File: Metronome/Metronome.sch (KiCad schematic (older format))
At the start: 48 parts, among them P1 CONN_01X02, P3 CONN_01X05, SW1 SW_PUSH, SW2 SW_PUSH, SW3 SW_PUSH, SW4 SW_PUSH, SW5 SW_PUSH, SW7 SWITCH_INV, T1 BSS138, T2 BSS83P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

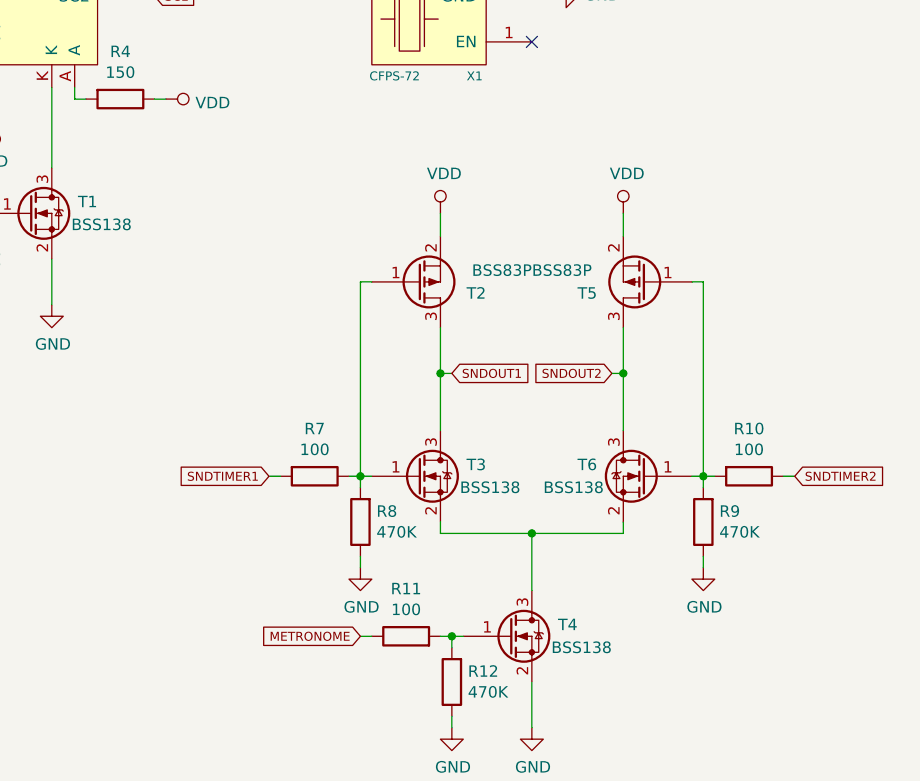
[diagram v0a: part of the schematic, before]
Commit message: PCB Simplification
SOme elements on PCB are unnecessary.
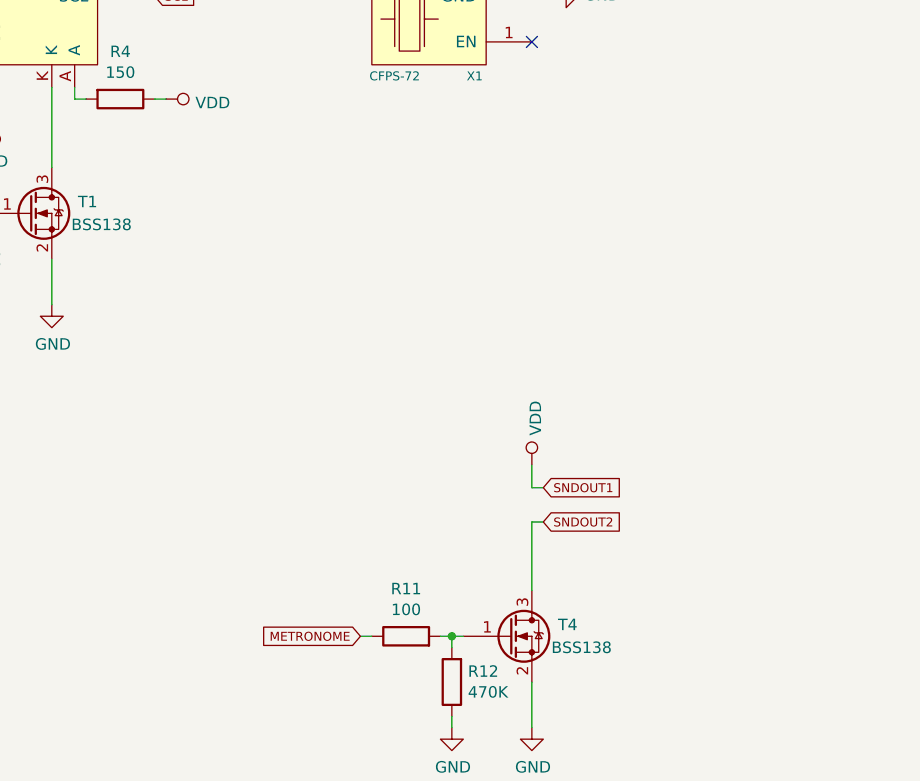
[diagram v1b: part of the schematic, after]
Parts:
- removed R10, R7: 100, Resistors_SMD:R_0603_HandSoldering, symbol R
- removed R8, R9: 470K, Resistors_SMD:R_0603_HandSoldering, symbol R
- removed T2, T5: BSS83P, TO_SOT_Packages_SMD:SOT-23_Handsoldering, symbol Q_PMOS_GSD
- removed T3, T6: BSS138, TO_SOT_Packages_SMD:SOT-23_Handsoldering, symbol Q_NMOS_GSD
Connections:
- net SNDOUT1 is gone; now on net VCC: R19.2
- net SNDOUT2: now also T4.3 (D)
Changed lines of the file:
@@
 Text GLabel 5200 2750 2    39   Input ~ 0
-METRONOME
-Text GLabel 8550 4000 0    39   Input ~ 0
 METRONOME
 $Comp
@@
 	-1   0    0    1
 $EndComp
-Text GLabel 8150 3300 0    39   Input ~ 0
-SNDTIMER1
 Text GLabel 5200 1650 2    39   Input ~ 0
 SNDTIMER1
-$Comp
-L VDD #PWR029
-U 1 1 57958A3B
-P 8900 2150
-F 0 "#PWR029" H 8900 2000 50  0001 C CNN
-F 1 "VDD" H 8917 2323 50  0000 C CNN
-F 2 "" H 8900 2150 50  0000 C CNN
-F 3 "" H 8900 2150 50  0000 C CNN
-	1    8900 2150
-	1    0    0    -1
-$EndComp
-$Comp
-L VDD #PWR030
-U 1 1 57958C88
-P 9700 2150
-F 0 "#PWR030" H 9700 2000 50  0001 C CNN
-F 1 "VDD" H 9717 2323 50  0000 C CNN
-F 2 "" H 9700 2150 50  0000 C CNN
-F 3 "" H 9700 2150 50  0000 C CNN
-	1    9700 2150
-	1    0    0    -1
-$EndComp
 $Comp
 L R R11
@@
 	1    0    0    -1
 $EndComp
-$Comp
-L R R7
-U 1 1 5795A29A
-P 8350 3300
-F 0 "R7" V 8143 3300 50  0000 C CNN
-F 1 "100" V 8234 3300 50  0000 C CNN
-F 2 "Resistors_SMD:R_0603_HandSoldering" V 8280 3300 50  0001 C CNN
-F 3 "" H 8350 3300 50  0000 C CNN
-	1    8350 3300
-	0    1    1    0
-$EndComp
-$Comp
-L R R8
-U 1 1 5795A4D7
-P 8550 3500
-F 0 "R8" H 8480 3454 50  0000 R CNN
-F 1 "470K" H 8480 3545 50  0000 R CNN
-F 2 "Resistors_SMD:R_0603_HandSoldering" V 8480 3500 50  0001 C CNN
-F 3 "" H 8550 3500 50  0000 C CNN
-	1    8550 3500
-	-1   0    0    1
-$EndComp
-$Comp
-L GND #PWR032
-U 1 1 5795A849
-P 8550 3700
-F 0 "#PWR032" H 8550 3450 50  0001 C CNN
-F 1 "GND" H 8555 3527 50  0000 C CNN
-F 2 "" H 8550 3700 50  0000 C CNN
-F 3 "" H 8550 3700 50  0000 C CNN
-	1    8550 3700
-	1    0    0    -1
-$EndComp
-$Comp
-L R R9
-U 1 1 5795B0C7
-P 10050 3500
-F 0 "R9" H 9980 3454 50  0000 R CNN
-F 1 "470K" H 9980 3545 50  0000 R CNN
-F 2 "Resistors_SMD:R_0603_HandSoldering" V 9980 3500 50  0001 C CNN
-F 3 "" H 10050 3500 50  0000 C CNN
-	1    10050 3500
-	-1   0    0    1
-$EndComp
-$Comp
-L GND #PWR033
-U 1 1 5795B1AB
-P 10050 3700
-F 0 "#PWR033" H 10050 3450 50  0001 C CNN
-F 1 "GND" H 10055 3527 50  0000 C CNN
-F 2 "" H 10050 3700 50  0000 C CNN
-F 3 "" H 10050 3700 50  0000 C CNN
-	1    10050 3700
-	1    0    0    -1
-$EndComp
-$Comp
-L R R10
-U 1 1 5795B70D
-P 10250 3300
-F 0 "R10" V 10043 3300 50  0000 C CNN
-F 1 "100" V 10134 3300 50  0000 C CNN
-F 2 "Resistors_SMD:R_0603_HandSoldering" V 10180 3300 50  0001 C CNN
-F 3 "" H 10250 3300 50  0000 C CNN
-	1    10250 3300
-	0    1    1    0
-$EndComp
-Text GLabel 10450 3300 2    39   Input ~ 0
-SNDTIMER2
-Text GLabel 8950 2850 2    39   Input ~ 0
-SNDOUT1
-Text GLabel 9650 2850 0    39   Input ~ 0
+Text GLabel 9350 3500 2    39   Input ~ 0
 SNDOUT2
 $Comp
@@
 $EndComp
 $Comp
-L Q_NMOS_GSD T3
-U 1 1 579D401D
-P 8800 3300
-F 0 "T3" H 9100 3350 50  0000 R CNN
-F 1 "BSS138" H 9250 3250 50  0000 R CNN
-F 2 "TO_SOT_Packages_SMD:SOT-23_Handsoldering" H 9000 3400 50  0001 C CNN
-F 3 "" H 8800 3300 50  0000 C CNN
-	1    8800 3300
-	1    0    0    -1
-$EndComp
-$Comp
-L Q_NMOS_GSD T6
-U 1 1 579D5110
-P 9800 3300
-F 0 "T6" H 10100 3350 50  0000 R CNN
-F 1 "BSS138" H 10250 3250 50  0000 R CNN
-F 2 "TO_SOT_Packages_SMD:SOT-23_Handsoldering" H 10000 3400 50  0001 C CNN
-F 3 "" H 9800 3300 50  0000 C CNN
-	1    9800 3300
-	-1   0    0    -1
-$EndComp
-$Comp
 L Q_NMOS_GSD T4
 U 1 1 579D66A3
@@
 	1    7100 2150
 	1    0    0    -1
-$EndComp
-$Comp
-L Q_PMOS_GSD T2
-U 1 1 579D8846
-P 8800 2450
-F 0 "T2" H 9100 2500 50  0000 R CNN
-F 1 "BSS83P" H 9300 2400 50  0000 R CNN
-F 2 "TO_SOT_Packages_SMD:SOT-23_Handsoldering" H 9000 2550 50  0001 C CNN
-F 3 "" H 8800 2450 50  0000 C CNN
-	1    8800 2450
-	1    0    0    1
-$EndComp
-$Comp
-L Q_PMOS_GSD T5
-U 1 1 579D9330
-P 9800 2450
-F 0 "T5" H 10100 2500 50  0000 R CNN
-F 1 "BSS83P" H 10300 2400 50  0000 R CNN
-F 2 "TO_SOT_Packages_SMD:SOT-23_Handsoldering" H 10000 2550 50  0001 C CNN
-F 3 "" H 9800 2450 50  0000 C CNN
-	1    9800 2450
-	-1   0    0    1
 $EndComp
 $Comp
@@
 	3750 2450 3700 2450
 Wire Wire Line
-	8900 2650 8900 3100
-Wire Wire Line
-	8900 2250 8900 2150
-Wire Wire Line
-	8550 2450 8600 2450
-Wire Wire Line
-	8550 3350 8550 2450
-Wire Wire Line
-	10050 2450 10050 3350
-Wire Wire Line
-	10000 2450 10050 2450
-Wire Wire Line
-	9700 2150 9700 2250
-Wire Wire Line
 	3750 2050 3700 2050
 Wire Wire Line
@@
 	5200 2150 5150 2150
 Wire Wire Line
-	8500 3300 8600 3300
-Wire Wire Line
 	8900 4000 9000 4000
 Wire Wire Line
 	8550 4000 8600 4000
-Wire Wire Line
-	10000 3300 10100 3300
-Wire Wire Line
-	8550 3700 8550 3650
-Connection ~ 8550 3300
-Wire Wire Line
-	10050 3700 10050 3650
-Connection ~ 10050 3300
-Wire Wire Line
-	8150 3300 8200 3300
-Wire Wire Line
-	10450 3300 10400 3300
-Wire Wire Line
-	9700 2650 9700 3100
-Connection ~ 8900 2850
-Connection ~ 9700 2850
-Wire Wire Line
-	8950 2850 8900 2850
-Wire Wire Line
-	9650 2850 9700 2850
 Wire Wire Line
 	8600 5200 9900 5200
@@
 Connection ~ 4750 3700
 Wire Wire Line
-	9300 3550 9300 3800
-Wire Wire Line
-	8900 3550 9700 3550
-Wire Wire Line
-	8900 3550 8900 3500
-Wire Wire Line
-	9700 3550 9700 3500
-Connection ~ 9300 3550
+	9300 3500 9300 3800
 Wire Wire Line
 	9300 4200 9300 4400
@@
 	5150 2750 5200 2750
 NoConn ~ 3700 2450
+Text GLabel 9350 3350 2    39   Input ~ 0
+SNDOUT1
+Text GLabel 8550 4000 0    39   Input ~ 0
+METRONOME
+Wire Wire Line
+	9350 3500 9300 3500
+Wire Wire Line
+	9300 3350 9350 3350
+Wire Wire Line
+	9300 3250 9300 3350
+$Comp
+L VDD #PWR?
+U 1 1 58AE1602
+P 9300 3250
+F 0 "#PWR?" H 9300 3100 50  0001 C CNN
+F 1 "VDD" V 9317 3378 50  0000 L CNN
+F 2 "" H 9300 3250 50  0000 C CNN
+F 3 "" H 9300 3250 50  0000 C CNN
+	1    9300 3250
+	1    0    0    -1
+$EndComp
 $EndSCHEMATC

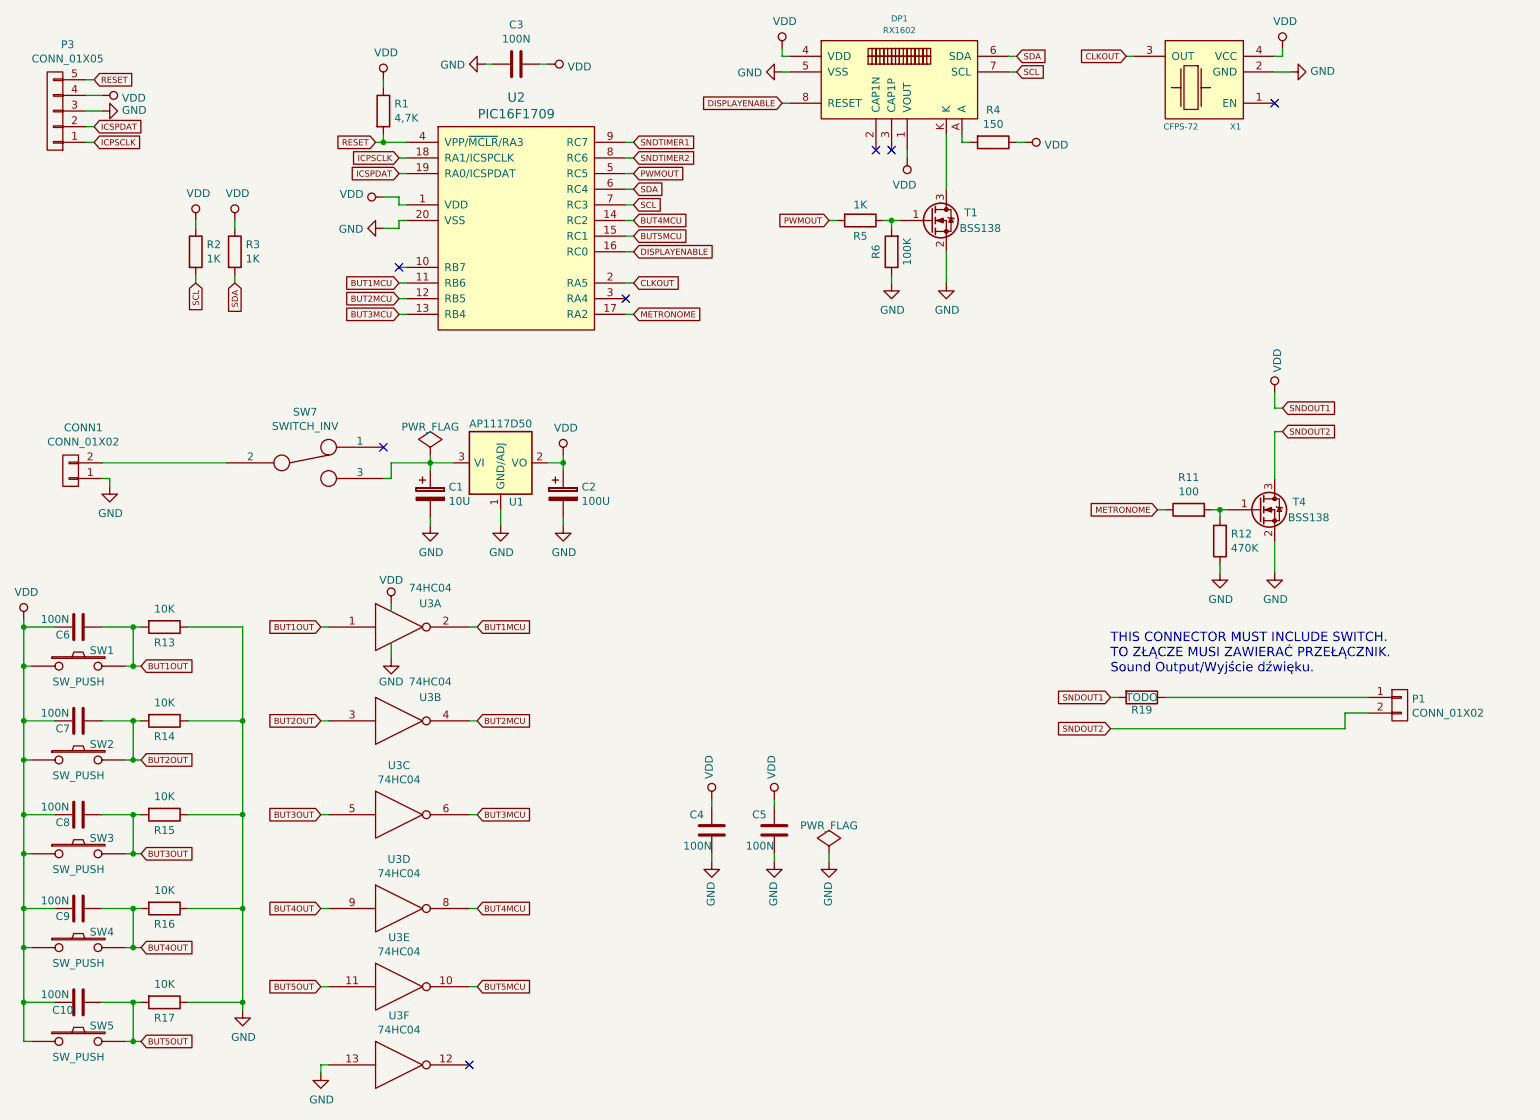
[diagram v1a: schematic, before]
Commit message: Deleting unnecessary traces on PCB
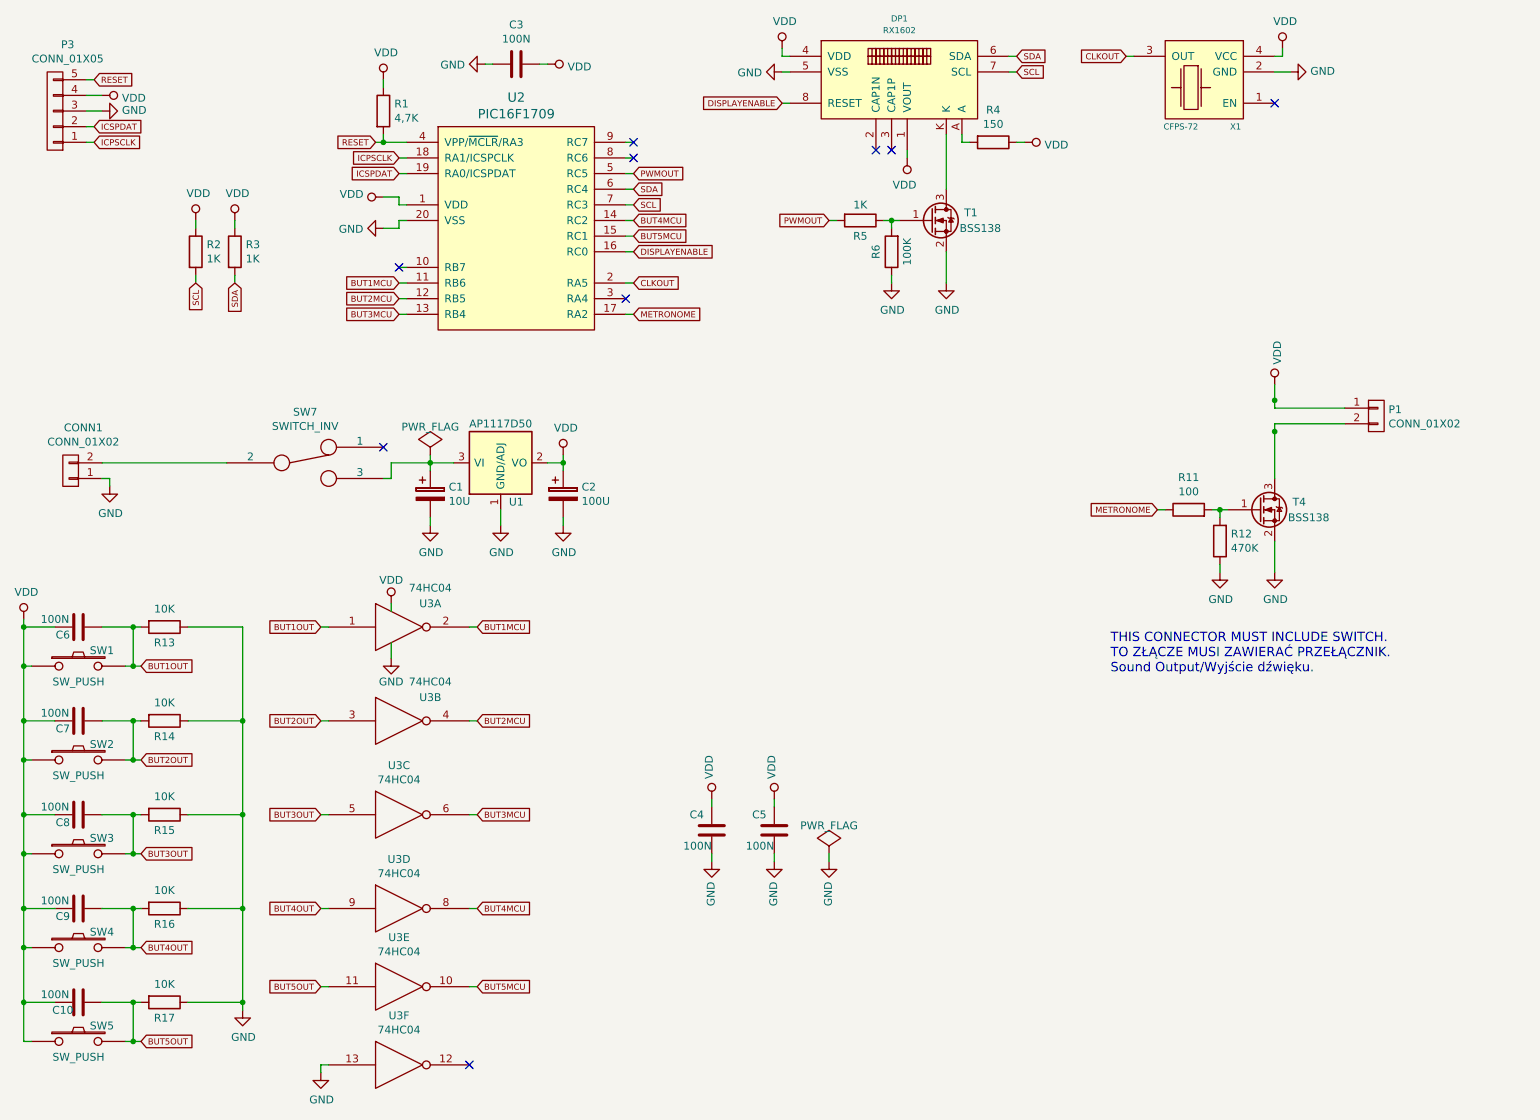
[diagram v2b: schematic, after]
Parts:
- removed R19: TODO, Resistors_SMD:R_0805_HandSoldering, symbol R
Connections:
- net VCC: now also P1.1 (P1)
- net SNDOUT2: no longer names the net of P1.2 (P2), T4.3 (D)
- net SNDTIMER1: no longer names the net of U2.9 (RC7)
- net SNDTIMER2: no longer names the net of U2.8 (RC6)
- no-connect marks 7 -> 9
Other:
- moved on the sheet: P1
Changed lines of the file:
@@
 Text GLabel 6150 1400 0    39   Input ~ 0
 DISPLAYENABLE
-Text GLabel 5200 1750 2    39   Input ~ 0
-SNDTIMER2
 $Comp
 L R R5
@@
 	-1   0    0    1
 $EndComp
-Text GLabel 5200 1650 2    39   Input ~ 0
-SNDTIMER1
 $Comp
 L R R11
@@
 $EndComp
 $Comp
-L GND #PWR031
+L GND #PWR029
 U 1 1 57959876
 P 9300 4400
-F 0 "#PWR031" H 9300 4150 50  0001 C CNN
+F 0 "#PWR029" H 9300 4150 50  0001 C CNN
 F 1 "GND" H 9305 4227 50  0000 C CNN
 F 2 "" H 9300 4400 50  0000 C CNN
@@
 	1    0    0    -1
 $EndComp
-Text GLabel 9350 3500 2    39   Input ~ 0
-SNDOUT2
 $Comp
 L R R12
@@
 $EndComp
 $Comp
-L GND #PWR034
+L GND #PWR030
 U 1 1 5796A8EC
 P 8950 4400
-F 0 "#PWR034" H 8950 4150 50  0001 C CNN
+F 0 "#PWR030" H 8950 4150 50  0001 C CNN
 F 1 "GND" H 8955 4227 50  0000 C CNN
 F 2 "" H 8950 4400 50  0000 C CNN
@@
 $EndComp
 $Comp
-L PWR_FLAG #FLG035
+L PWR_FLAG #FLG031
 U 1 1 5797F436
 P 3900 3650
-F 0 "#FLG035" H 3900 3745 50  0001 C CNN
+F 0 "#FLG031" H 3900 3745 50  0001 C CNN
 F 1 "PWR_FLAG" H 3900 3830 50  0000 C CNN
 F 2 "" H 3900 3650 50  0000 C CNN
@@
 NoConn ~ 3600 3600
 $Comp
-L GND #PWR036
+L GND #PWR032
 U 1 1 57981ADB
 P 6450 6250
-F 0 "#PWR036" H 6450 6000 50  0001 C CNN
+F 0 "#PWR032" H 6450 6000 50  0001 C CNN
 F 1 "GND" V 6455 6122 50  0000 R CNN
 F 2 "" H 6450 6250 50  0000 C CNN
@@
 $EndComp
 $Comp
-L PWR_FLAG #FLG037
+L PWR_FLAG #FLG033
 U 1 1 57981B5C
 P 6450 6200
-F 0 "#FLG037" H 6450 6295 50  0001 C CNN
+F 0 "#FLG033" H 6450 6295 50  0001 C CNN
 F 1 "PWR_FLAG" H 6450 6380 50  0000 C CNN
 F 2 "" H 6450 6200 50  0000 C CNN
@@
 	1    0    0    -1
 $EndComp
-Text GLabel 8250 5200 0    39   Input ~ 0
-SNDOUT1
-Text GLabel 8250 5400 0    39   Input ~ 0
-SNDOUT2
-$Comp
-L VDD #PWR038
+$Comp
+L VDD #PWR034
 U 1 1 57983B16
 P 3650 4600
-F 0 "#PWR038" H 3650 4450 50  0001 C CNN
+F 0 "#PWR034" H 3650 4450 50  0001 C CNN
 F 1 "VDD" H 3650 4750 50  0000 C CNN
 F 2 "" H 3650 4600 50  0000 C CNN
@@
 $EndComp
 $Comp
-L GND #PWR039
+L GND #PWR035
 U 1 1 5798475D
 P 3650 4950
-F 0 "#PWR039" H 3650 4700 50  0001 C CNN
+F 0 "#PWR035" H 3650 4700 50  0001 C CNN
 F 1 "GND" H 3650 4800 50  0000 C CNN
 F 2 "" H 3650 4950 50  0000 C CNN
@@
 	1    0    0    -1
 $EndComp
-$Comp
-L R R19
-U 1 1 579DECB2
-P 8450 5200
-F 0 "R19" V 8530 5200 50  0000 C CNN
-F 1 "TODO" V 8450 5200 50  0000 C CNN
-F 2 "Resistors_SMD:R_0805_HandSoldering" V 8380 5200 50  0001 C CNN
-F 3 "" H 8450 5200 50  0000 C CNN
-	1    8450 5200
-	0    1    1    0
-$EndComp
 NoConn ~ 5150 2650
 Text Notes 8250 5050 0    60   ~ 0
@@
 L CONN_01X02 P1
 U 1 1 57A646B0
-P 10100 5250
-F 0 "P1" H 10178 5291 50  0000 L CNN
-F 1 "CONN_01X02" H 10178 5200 50  0000 L CNN
-F 2 "Pin_Headers:Pin_Header_Straight_1x02" H 10100 5250 50  0001 C CNN
-F 3 "" H 10100 5250 50  0000 C CNN
-	1    10100 5250
+P 9950 3400
+F 0 "P1" H 10028 3441 50  0000 L CNN
+F 1 "CONN_01X02" H 10028 3350 50  0000 L CNN
+F 2 "Pin_Headers:Pin_Header_Straight_1x02" H 9950 3400 50  0001 C CNN
+F 3 "" H 9950 3400 50  0000 C CNN
+	1    9950 3400
 	1    0    0    -1
 $EndComp
@@
 $EndComp
 $Comp
-L GND #PWR040
+L GND #PWR036
 U 1 1 57BF3294
 P 1850 3850
-F 0 "#PWR040" H 1850 3600 50  0001 C CNN
+F 0 "#PWR036" H 1850 3600 50  0001 C CNN
 F 1 "GND" H 1855 3677 50  0000 C CNN
 F 2 "" H 1850 3850 50  0000 C CNN
@@
 $EndComp
 Wire Wire Line
-	8250 5200 8300 5200
-Wire Wire Line
 	3750 2550 3700 2550
 Wire Wire Line
@@
 	8550 4000 8600 4000
 Wire Wire Line
-	8600 5200 9900 5200
-Wire Wire Line
 	8950 4000 8950 4050
 Connection ~ 8950 4000
@@
 Connection ~ 4750 3700
 Wire Wire Line
-	9300 3500 9300 3800
+	9300 3450 9300 3800
 Wire Wire Line
 	9300 4200 9300 4400
-Wire Wire Line
-	9900 5300 9750 5300
-Wire Wire Line
-	9750 5300 9750 5400
-Wire Wire Line
-	9750 5400 8250 5400
 Wire Wire Line
 	6950 1750 6950 1700
@@
 	5150 2750 5200 2750
 NoConn ~ 3700 2450
-Text GLabel 9350 3350 2    39   Input ~ 0
-SNDOUT1
 Text GLabel 8550 4000 0    39   Input ~ 0
 METRONOME
 Wire Wire Line
-	9350 3500 9300 3500
-Wire Wire Line
-	9300 3350 9350 3350
-Wire Wire Line
-	9300 3250 9300 3350
-$Comp
-L VDD #PWR?
+	9300 3200 9300 3350
+$Comp
+L VDD #PWR037
 U 1 1 58AE1602
-P 9300 3250
-F 0 "#PWR?" H 9300 3100 50  0001 C CNN
-F 1 "VDD" V 9317 3378 50  0000 L CNN
-F 2 "" H 9300 3250 50  0000 C CNN
-F 3 "" H 9300 3250 50  0000 C CNN
-	1    9300 3250
-	1    0    0    -1
-$EndComp
+P 9300 3200
+F 0 "#PWR037" H 9300 3050 50  0001 C CNN
+F 1 "VDD" V 9317 3328 50  0000 L CNN
+F 2 "" H 9300 3200 50  0000 C CNN
+F 3 "" H 9300 3200 50  0000 C CNN
+	1    9300 3200
+	1    0    0    -1
+$EndComp
+NoConn ~ 5200 1650
+NoConn ~ 5200 1750
+Wire Wire Line
+	9300 3350 9750 3350
+Connection ~ 9300 3300
+Wire Wire Line
+	9750 3450 9300 3450
+Connection ~ 9300 3500
 $EndSCHEMATC

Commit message: Fixes on PCB
New PCB version is not yet ready.
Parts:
- U2: footprint SMD_Packages:SSOP-20 -> Housings_SSOP:SSOP-20_5.3x7.2mm_Pitch0.65mm
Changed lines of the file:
@@
 F 0 "U2" H 4450 3037 60  0000 C CNN
 F 1 "PIC16F1709" H 4450 2931 60  0000 C CNN
-F 2 "SMD_Packages:SSOP-20" H 4450 2200 60  0001 C CNN
+F 2 "Housings_SSOP:SSOP-20_5.3x7.2mm_Pitch0.65mm" H 4450 2200 60  0001 C CNN
 F 3 "" H 4450 2200 60  0000 C CNN
 	1    4450 2200
